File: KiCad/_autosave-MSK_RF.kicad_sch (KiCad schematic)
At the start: 69 parts, among them J3 Conn_01x12, J4 Conn_Coaxial, SW2 SW_Push, SW3 SW_Push, U1 STM32WLE5CCU6, U2 ADG918BRM, U3 TLV70233_SOT23-5, Y1 32.768 kHz, Y2 32MHz

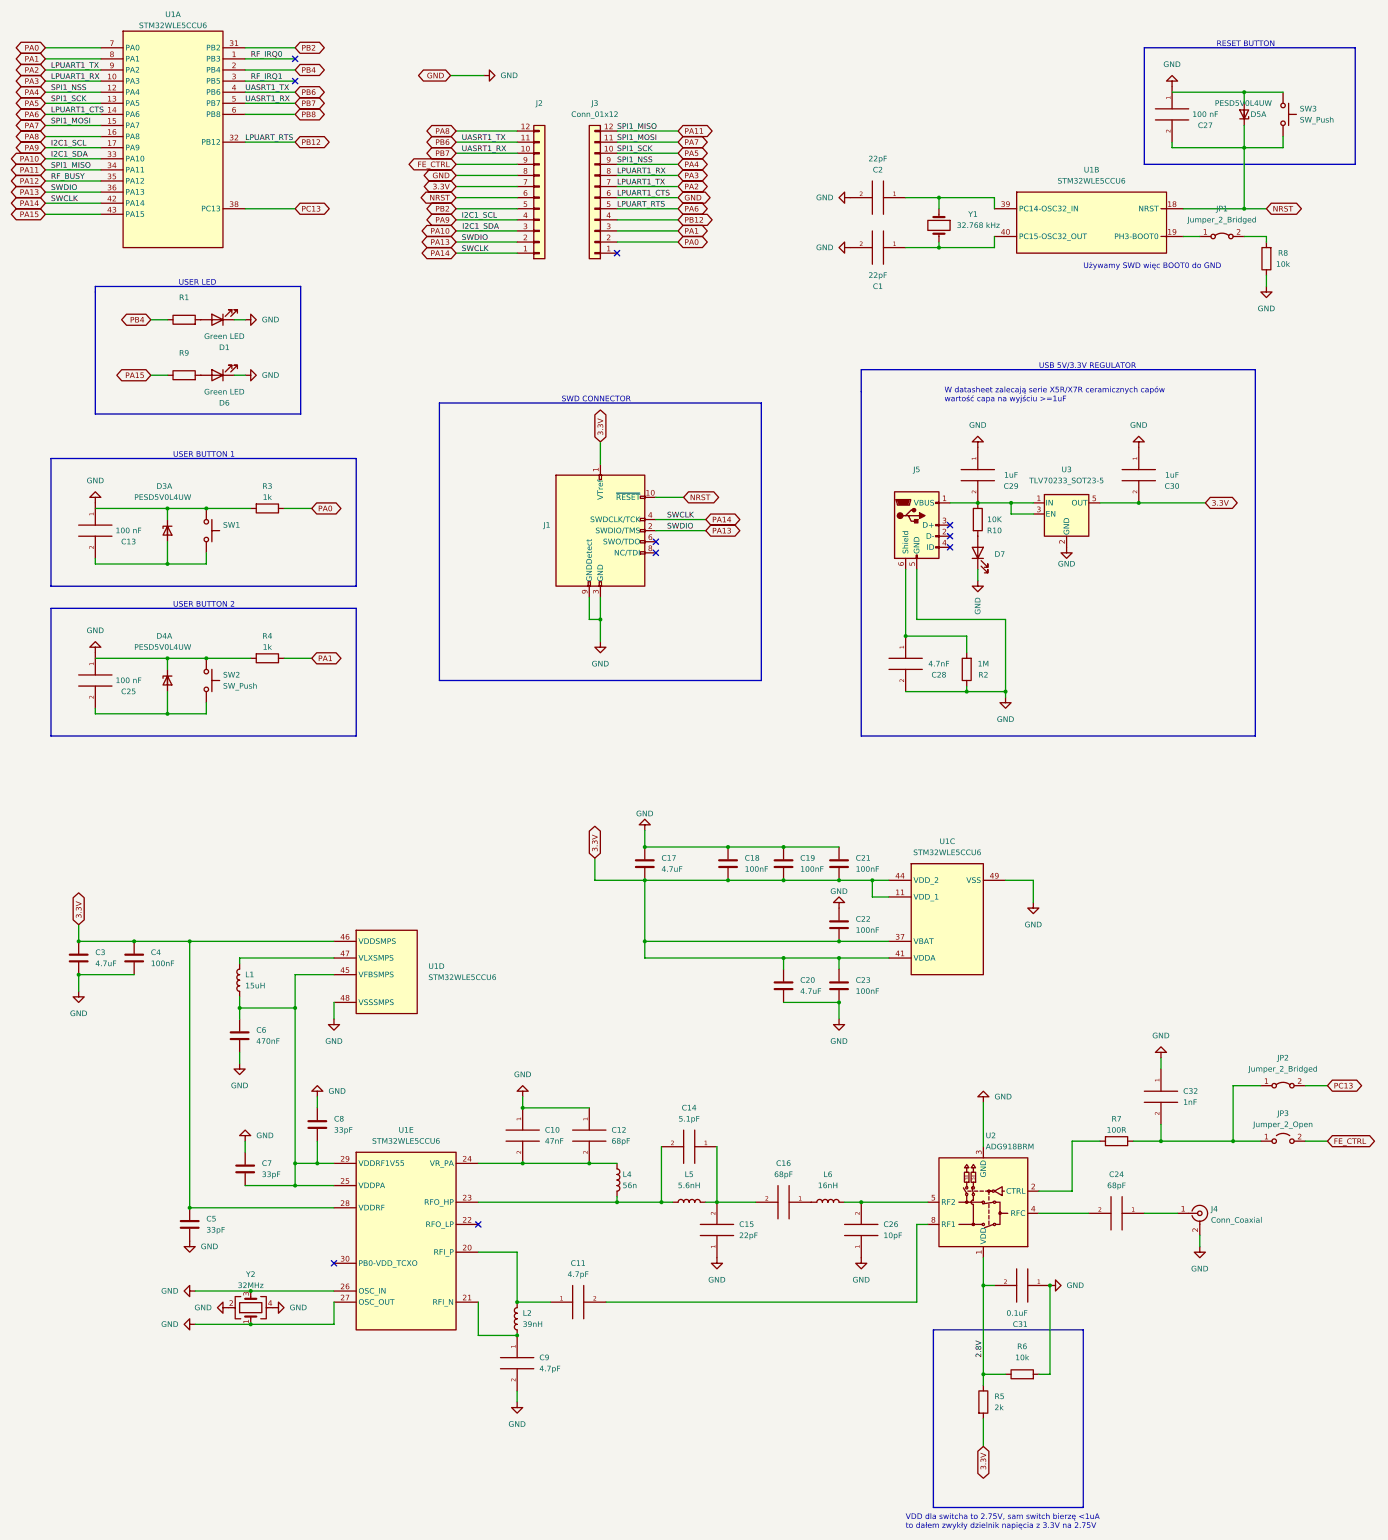
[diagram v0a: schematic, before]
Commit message: finished schematic with footprint
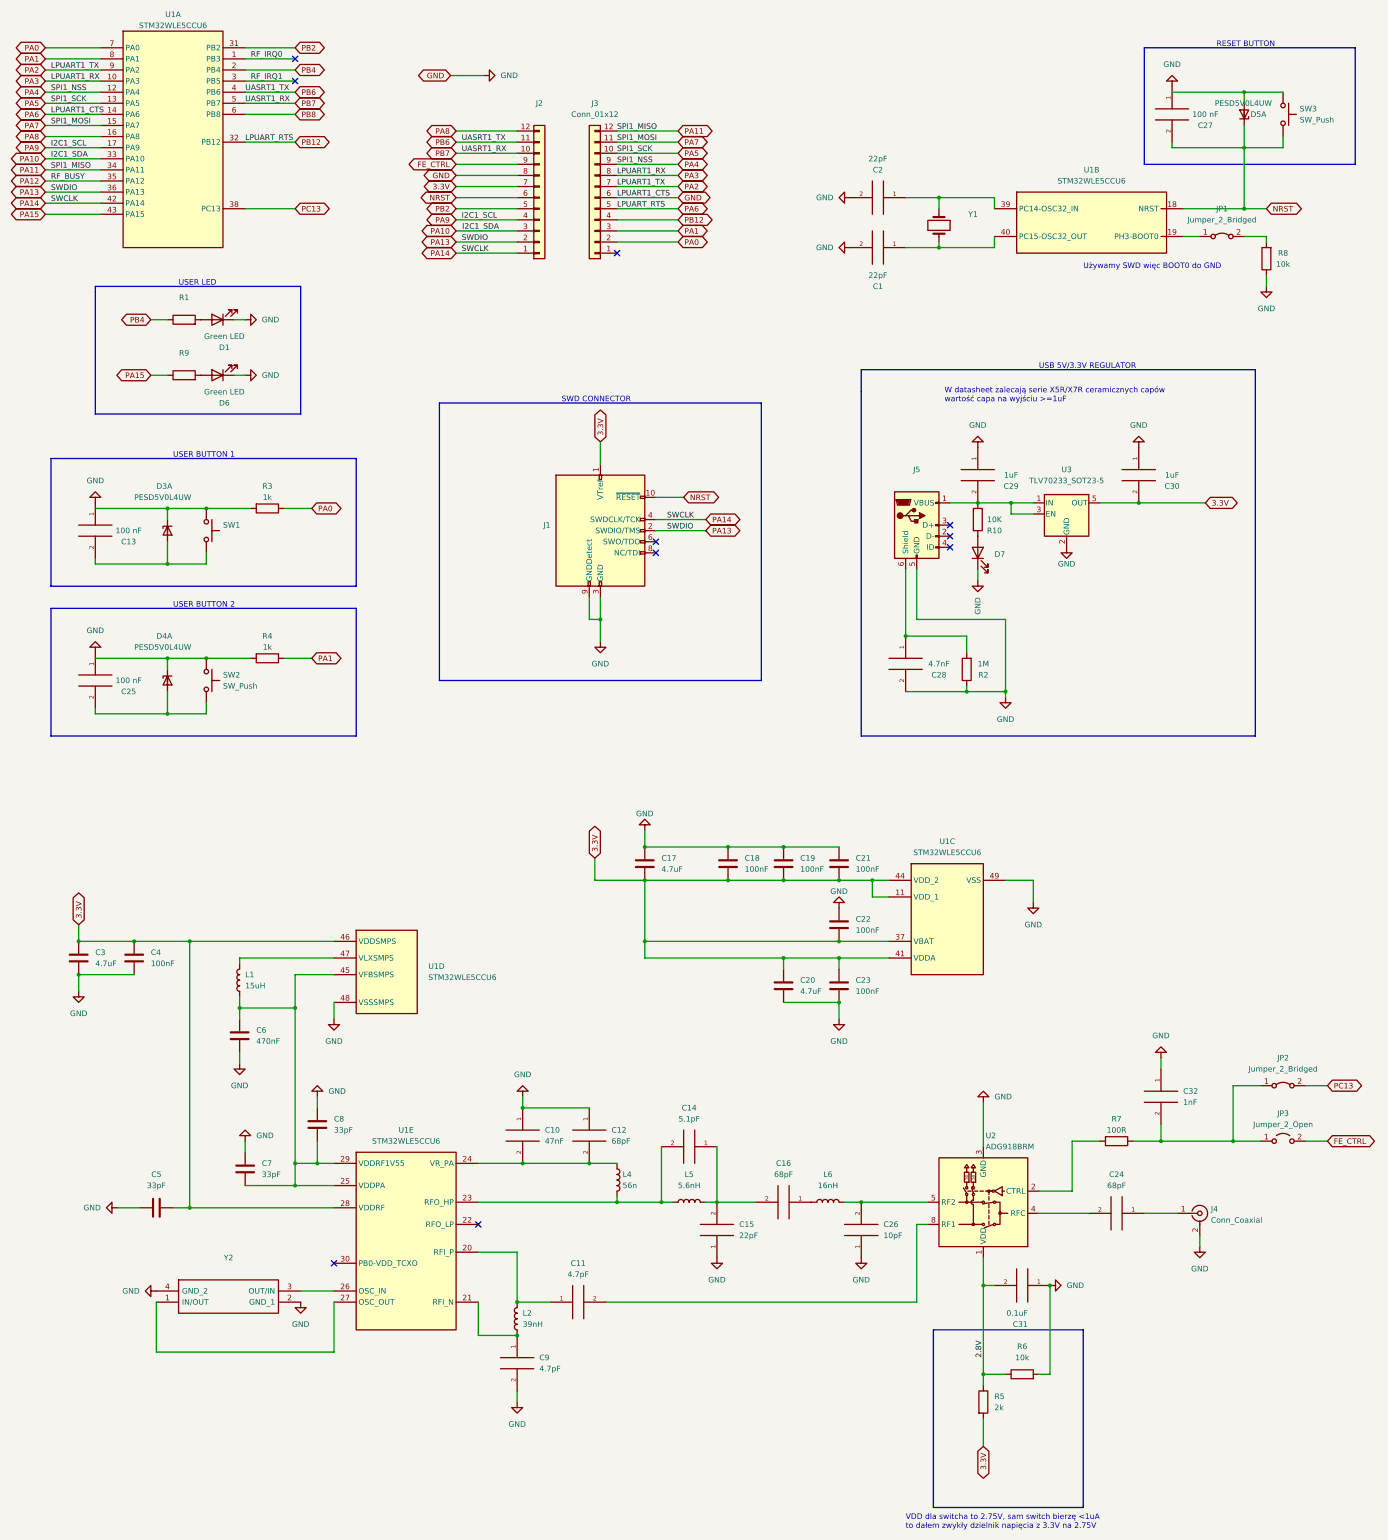
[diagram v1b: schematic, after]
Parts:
- removed Y2: 32MHz, symbol Device:Crystal_GND24
- added Y2: (no value), symbol SamacSys_Parts:ECS-320-8-37-CKM-TR3
- Y1: value 32.768 kHz -> (none); footprint Oscillator:Oscillator_SMD_Abracon_ASDMB-4Pin_2.5x2.0mm -> (none)
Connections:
- net 3.3V: now also C5.1; no longer C5.2
- net GND: now also C5.2, Y2.2 (GND_1), Y2.4 (GND_2); no longer C5.1, U1.26 (OSC_IN), U1.27 (OSC_OUT)
- new net: U1.27 (OSC_OUT), Y2.1 (IN/OUT)
- new net: U1.26 (OSC_IN), Y2.3 (OUT/IN)
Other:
- moved on the sheet: C5
